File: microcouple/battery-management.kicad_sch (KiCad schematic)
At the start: 0 parts

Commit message: Finalize battery management
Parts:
- added C16, C17, C18, C19: 4.7uF, Capacitor_SMD:C_0805_2012Metric_Pad1.18x1.45mm_HandSolder, symbol Device:C
- added D66: SB5H100, Diode_SMD:D_SMB_Handsoldering, symbol Diode:SB5H100
- added D67: Charging, LED_SMD:LED_0805_2012Metric_Pad1.15x1.40mm_HandSolder, symbol Device:LED
- added D68: Done, LED_SMD:LED_0805_2012Metric_Pad1.15x1.40mm_HandSolder, symbol Device:LED
- added L1: 2.2uH, symbol Device:L
- added Q2: AO3415, Package_TO_SOT_SMD:SOT-23_Handsoldering, symbol Transistor_FET:AO3401A
- added R15: 100k, Resistor_SMD:R_0805_2012Metric_Pad1.20x1.40mm_HandSolder, symbol Device:R_US
- added R16, R17: 470R, Resistor_SMD:R_0805_2012Metric_Pad1.20x1.40mm_HandSolder, symbol Device:R_US
- added R18: 10k, Resistor_SMD:R_0805_2012Metric_Pad1.20x1.40mm_HandSolder, symbol Device:R_US
- added U5: MCP73831-2-OT, Package_TO_SOT_SMD:SOT-23-5_HandSoldering, symbol Battery_Management:MCP73831-2-OT
- added U6: LM3671MFX, Package_TO_SOT_SMD:TSOT-23-5_HandSoldering, symbol Regulator_Switching:LM3670MF
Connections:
- new net: D67.2 (A), R16.1
- new net: L1.1, U6.5 (SW)
- new net: C16.1, D66.1 (K), Q2.2 (S), U6.1 (Vin), U6.3 (EN)
- new net: D68.1 (K), R17.2
- new net: R18.1, U5.5 (PROG)
- new net +3.3V: C17.1, L1.2, U6.4 (FB)
- new net +BATT: C18.1, Q2.3 (D), U5.3 (V_{BAT})
- new net Charge Status: D67.1 (K), D68.2 (A), U5.1 (STAT)
- new net GND: C16.2, C17.2, C18.2, C19.2, R15.2, R17.1, R18.2, U5.2 (V_{SS}), U6.2 (GND)
- new net VBUS: C19.1, D66.2 (A), Q2.1 (G), R15.1, R16.2, U5.4 (V_{DD})
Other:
- note added: "https://blog.zakkemble.net/a-lithium-battery-charger-with-load-sharing/"

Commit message: Preliminary Schematic
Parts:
- C13: renamed from C18; footprint Capacitor_SMD:C_0805_2012Metric_Pad1.18x1.45mm_HandSolder -> Capacitor_SMD:C_0402_1005Metric
- C14: renamed from C19; footprint Capacitor_SMD:C_0805_2012Metric_Pad1.18x1.45mm_HandSolder -> Capacitor_SMD:C_0402_1005Metric
- C15: renamed from C16; footprint Capacitor_SMD:C_0805_2012Metric_Pad1.18x1.45mm_HandSolder -> Capacitor_SMD:C_0402_1005Metric
- C16: renamed from C17; footprint Capacitor_SMD:C_0805_2012Metric_Pad1.18x1.45mm_HandSolder -> Capacitor_SMD:C_0402_1005Metric
- D66: renamed from D67; footprint LED_SMD:LED_0805_2012Metric_Pad1.15x1.40mm_HandSolder -> LED_SMD:LED_0201_0603Metric
- D67: renamed from D68; footprint LED_SMD:LED_0805_2012Metric_Pad1.15x1.40mm_HandSolder -> LED_SMD:LED_0201_0603Metric
- L1: footprint (none) -> Inductor_SMD:L_1008_2520Metric
- R4: renamed from R16; value 470R -> 1.5k; footprint Resistor_SMD:R_0805_2012Metric_Pad1.20x1.40mm_HandSolder -> Resistor_SMD:R_0201_0603Metric
- R5: renamed from R18; footprint Resistor_SMD:R_0805_2012Metric_Pad1.20x1.40mm_HandSolder -> Resistor_SMD:R_0201_0603Metric
- R6: renamed from R17; value 470R -> 1.5k; footprint Resistor_SMD:R_0805_2012Metric_Pad1.20x1.40mm_HandSolder -> Resistor_SMD:R_0201_0603Metric
- R7: renamed from R15; footprint Resistor_SMD:R_0805_2012Metric_Pad1.20x1.40mm_HandSolder -> Resistor_SMD:R_0201_0603Metric
- renumbered D66 to D68, Q2 to Q1, U5 to U4, U6 to U5
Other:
- note removed: "https://blog.zakkemble.net/a-lithium-battery-charger-with-load-sharing/"
- company: (none) -> George Sleen
- moved on the sheet: C13, C14, C15, C16, D66, D67, D68, L1, Q1, R4, R5, R6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

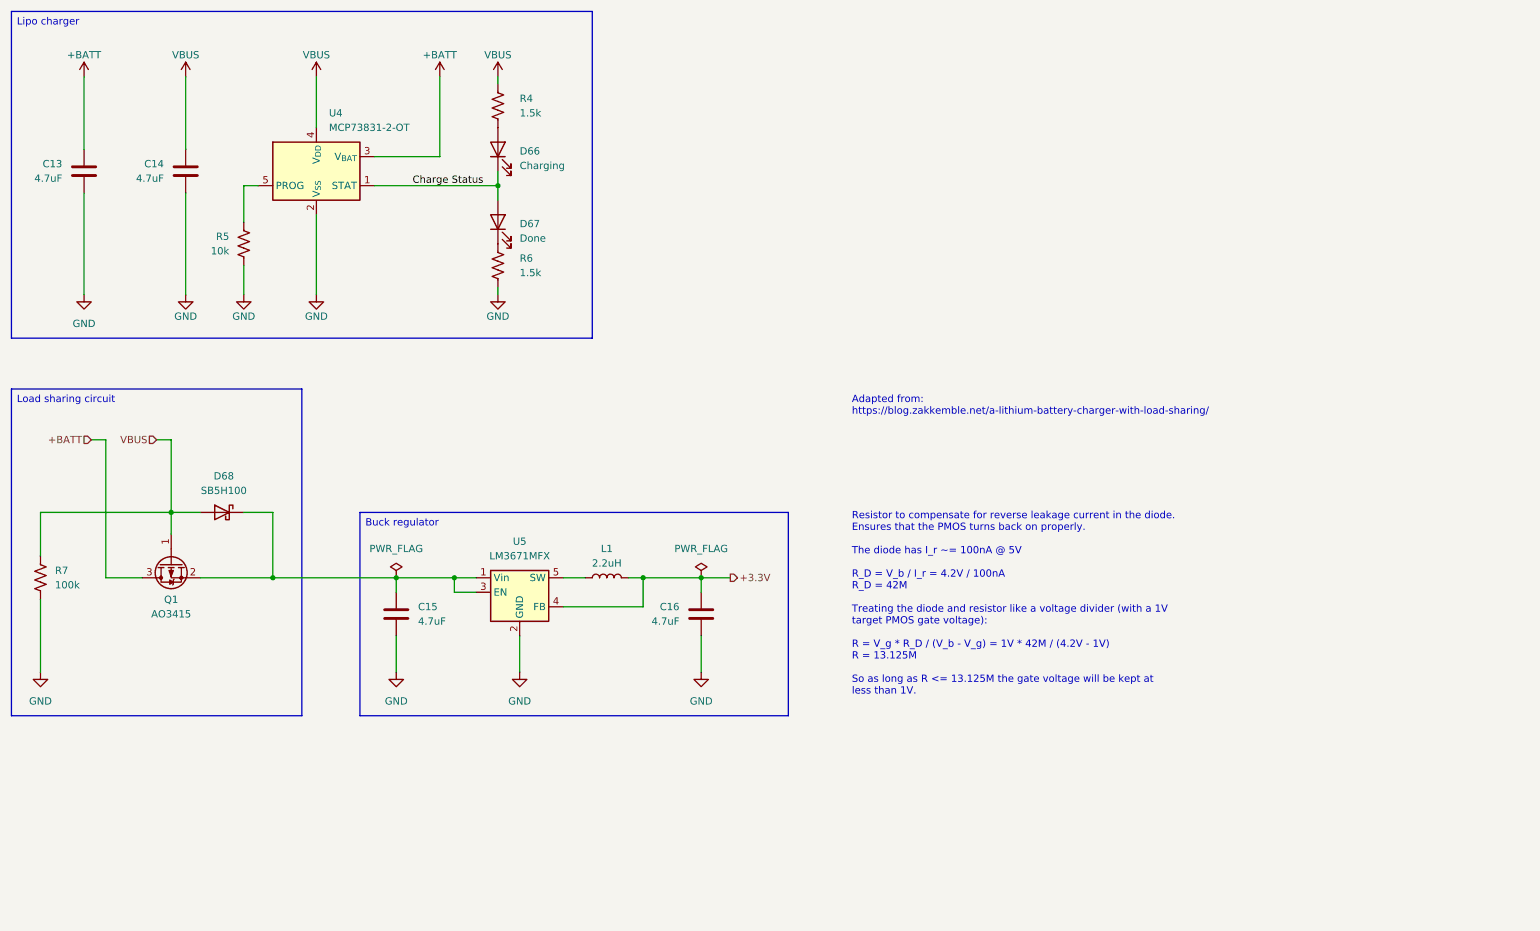
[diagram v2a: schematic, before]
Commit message: Switch THT IR components to SMD ones
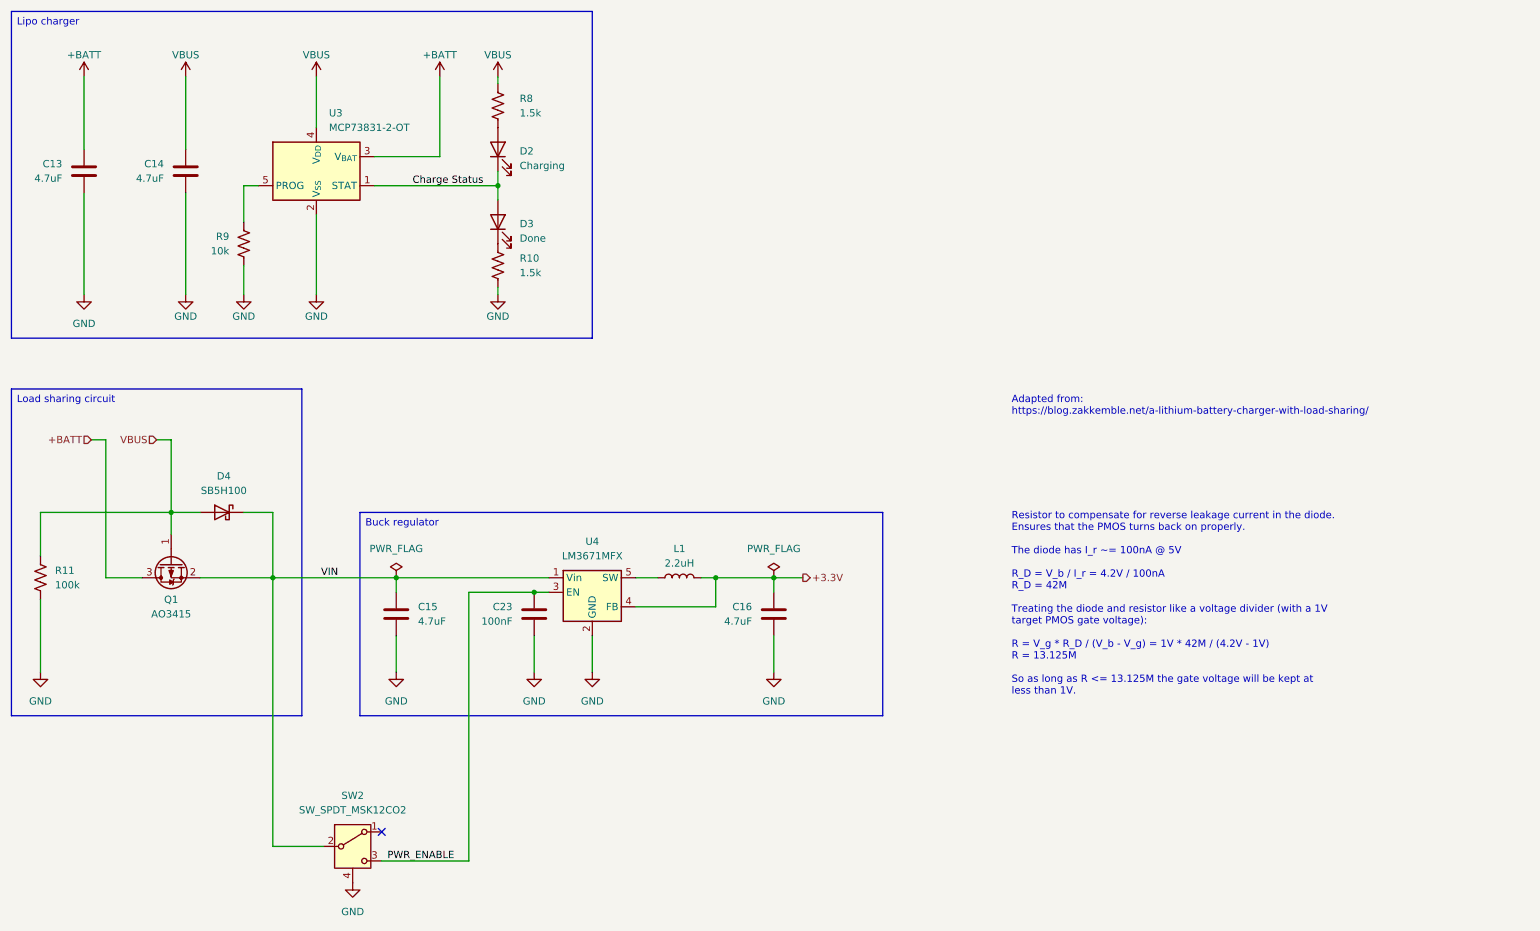
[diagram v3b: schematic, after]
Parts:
- added C23: 100nF, Capacitor_SMD:C_0201_0603Metric, symbol Device:C
- added SW2: SW_SPDT_MSK12CO2, GS_Switches:MSK12CO2, symbol GS_Switches:SW_SPDT_MSK12CO2
- D4: renamed from D68; footprint Diode_SMD:D_SMB_Handsoldering -> Diode_SMD:D_SMB
- U3: renamed from U4; footprint Package_TO_SOT_SMD:SOT-23-5_HandSoldering -> Package_TO_SOT_SMD:SOT-23-5
- U4: renamed from U5; footprint Package_TO_SOT_SMD:TSOT-23-5_HandSoldering -> Package_TO_SOT_SMD:TSOT-23-5
- renumbered D66 to D2, D67 to D3, R6 to R10, R7 to R11, R4 to R8, R5 to R9
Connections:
- net GND: now also C23.2, SW2.4 (Shield)
- net VIN: now reaches C15.1, D4.1 (K), Q1.2 (S), U4.1 (Vin)
- net VIN: now also SW2.2 (B); no longer U4.3 (EN)
- new net PWR_ENABLE: C23.1, SW2.3 (C), U4.3 (EN)
- no-connect marks 0 -> 1
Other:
- moved on the sheet: C16, L1, U4

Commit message: Preliminary layout
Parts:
- Q1: footprint Package_TO_SOT_SMD:SOT-23_Handsoldering -> Package_TO_SOT_SMD:SOT-23
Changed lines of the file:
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@@
 			)
 		)
-		(property "Footprint" "Package_TO_SOT_SMD:SOT-23_Handsoldering"
+		(property "Footprint" "Package_TO_SOT_SMD:SOT-23"
 			(at 55.245 127 0)
 			(effects

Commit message: Draft layout
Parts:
- renumbered C23 to C16, C16 to C17, D4 to D2, D2 to D3, D3 to D4, R9 to R10, R8 to R11, R10 to R12, R11 to R9
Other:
- title: (none) -> Battery Management
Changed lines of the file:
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@@
 	(paper "A4")
 	(title_block
+		(title "Battery Management")
 		(rev "A")
 		(company "George Sleen")
@@
 		(dnp no)
 		(fields_autoplaced yes)
-		(property "Reference" "D2"
+		(property "Reference" "D3"
 			(at 114.3 49.8474 90)
 			(effects
@@
 			(project ""
 				(path "/d639f16d-aedb-4af6-af94-94ea25244267/528e496b-ccc4-4c28-b7b2-36634450f252"
-					(reference "D2")
+					(reference "D3")
 					(unit 1)
 				)
@@
 		(on_board yes)
 		(dnp no)
-		(property "Reference" "#PWR049"
+		(property "Reference" "#PWR052"
 			(at 110.49 81.28 0)
 			(effects
@@
 			(project "microcouple"
 				(path "/d639f16d-aedb-4af6-af94-94ea25244267/528e496b-ccc4-4c28-b7b2-36634450f252"
-					(reference "#PWR049")
+					(reference "#PWR052")
 					(unit 1)
 				)
@@
 		(on_board yes)
 		(dnp no)
-		(property "Reference" "#PWR040"
+		(property "Reference" "#PWR041"
 			(at 38.1 40.64 0)
 			(effects
@@
 			(project "microcouple"
 				(path "/d639f16d-aedb-4af6-af94-94ea25244267/528e496b-ccc4-4c28-b7b2-36634450f252"
-					(reference "#PWR040")
+					(reference "#PWR041")
 					(unit 1)
 				)
@@
 		(on_board yes)
 		(dnp no)
-		(property "Reference" "R8"
+		(property "Reference" "R11"
 			(at 114.3 40.64 0)
 			(effects
@@
 			(project ""
 				(path "/d639f16d-aedb-4af6-af94-94ea25244267/528e496b-ccc4-4c28-b7b2-36634450f252"
-					(reference "R8")
+					(reference "R11")
 					(unit 1)
 				)
@@
 		(on_board yes)
 		(dnp no)
-		(property "Reference" "R10"
+		(property "Reference" "R12"
 			(at 114.3 68.58 0)
 			(effects
@@
 			(project "microcouple"
 				(path "/d639f16d-aedb-4af6-af94-94ea25244267/528e496b-ccc4-4c28-b7b2-36634450f252"
-					(reference "R10")
+					(reference "R12")
 					(unit 1)
 				)
@@
 		(on_board yes)
 		(dnp no)
-		(property "Reference" "D4"
+		(property "Reference" "D2"
 			(at 62.5475 106.68 0)
 			(effects
@@
 			(project ""
 				(path "/d639f16d-aedb-4af6-af94-94ea25244267/528e496b-ccc4-4c28-b7b2-36634450f252"
-					(reference "D4")
+					(reference "D2")
 					(unit 1)
 				)
@@
 		(dnp no)
 		(fields_autoplaced yes)
-		(property "Reference" "C23"
+		(property "Reference" "C16"
 			(at 113.03 129.5399 0)
 			(effects
@@
 			(project "microcouple"
 				(path "/d639f16d-aedb-4af6-af94-94ea25244267/528e496b-ccc4-4c28-b7b2-36634450f252"
-					(reference "C23")
+					(reference "C16")
 					(unit 1)
 				)
@@
 		(on_board yes)
 		(dnp no)
-		(property "Reference" "#PWR048"
+		(property "Reference" "#PWR047"
 			(at 78.74 81.28 0)
 			(effects
@@
 			(project ""
 				(path "/d639f16d-aedb-4af6-af94-94ea25244267/528e496b-ccc4-4c28-b7b2-36634450f252"
-					(reference "#PWR048")
+					(reference "#PWR047")
 					(unit 1)
 				)
@@
 		(on_board yes)
 		(dnp no)
-		(property "Reference" "#PWR042"
+		(property "Reference" "#PWR046"
 			(at 78.74 40.64 0)
 			(effects
@@
 			(project ""
 				(path "/d639f16d-aedb-4af6-af94-94ea25244267/528e496b-ccc4-4c28-b7b2-36634450f252"
-					(reference "#PWR042")
+					(reference "#PWR046")
 					(unit 1)
 				)
@@
 		(dnp no)
 		(fields_autoplaced yes)
-		(property "Reference" "#PWR050"
+		(property "Reference" "#PWR040"
 			(at 30.48 147.32 0)
 			(effects
@@
 			(project "microcouple"
 				(path "/d639f16d-aedb-4af6-af94-94ea25244267/528e496b-ccc4-4c28-b7b2-36634450f252"
-					(reference "#PWR050")
+					(reference "#PWR040")
 					(unit 1)
 				)
@@
 		(dnp no)
 		(fields_autoplaced yes)
-		(property "Reference" "#PWR053"
+		(property "Reference" "#PWR055"
 			(at 158.75 147.32 0)
 			(effects
@@
 			(project "microcouple"
 				(path "/d639f16d-aedb-4af6-af94-94ea25244267/528e496b-ccc4-4c28-b7b2-36634450f252"
-					(reference "#PWR053")
+					(reference "#PWR055")
 					(unit 1)
 				)
@@
 		(dnp no)
 		(fields_autoplaced yes)
-		(property "Reference" "#PWR051"
+		(property "Reference" "#PWR049"
 			(at 92.71 147.32 0)
 			(effects
@@
 			(project "microcouple"
 				(path "/d639f16d-aedb-4af6-af94-94ea25244267/528e496b-ccc4-4c28-b7b2-36634450f252"
-					(reference "#PWR051")
+					(reference "#PWR049")
 					(unit 1)
 				)
@@
 		(on_board yes)
 		(dnp no)
-		(property "Reference" "R11"
+		(property "Reference" "R9"
 			(at 33.02 123.1899 0)
 			(effects
@@
 			(project ""
 				(path "/d639f16d-aedb-4af6-af94-94ea25244267/528e496b-ccc4-4c28-b7b2-36634450f252"
-					(reference "R11")
+					(reference "R9")
 					(unit 1)
 				)
@@
 		(dnp no)
 		(fields_autoplaced yes)
-		(property "Reference" "#PWR074"
+		(property "Reference" "#PWR048"
 			(at 85.09 184.15 0)
 			(effects
@@
 			(project ""
 				(path "/d639f16d-aedb-4af6-af94-94ea25244267/528e496b-ccc4-4c28-b7b2-36634450f252"
-					(reference "#PWR074")
+					(reference "#PWR048")
 					(unit 1)
 				)
@@
 		(on_board yes)
 		(dnp no)
-		(property "Reference" "D3"
+		(property "Reference" "D4"
 			(at 114.3 62.5474 90)
 			(effects
@@
 			(project "microcouple"
 				(path "/d639f16d-aedb-4af6-af94-94ea25244267/528e496b-ccc4-4c28-b7b2-36634450f252"
-					(reference "D3")
+					(reference "D4")
 					(unit 1)
 				)
@@
 		(dnp no)
 		(fields_autoplaced yes)
-		(property "Reference" "#PWR052"
+		(property "Reference" "#PWR054"
 			(at 127 147.32 0)
 			(effects
@@
 			(project "microcouple"
 				(path "/d639f16d-aedb-4af6-af94-94ea25244267/528e496b-ccc4-4c28-b7b2-36634450f252"
-					(reference "#PWR052")
+					(reference "#PWR054")
 					(unit 1)
 				)
@@
 		(on_board yes)
 		(dnp no)
-		(property "Reference" "C16"
+		(property "Reference" "C17"
 			(at 154.94 129.5399 0)
 			(effects
@@
 			(project ""
 				(path "/d639f16d-aedb-4af6-af94-94ea25244267/528e496b-ccc4-4c28-b7b2-36634450f252"
-					(reference "C16")
+					(reference "C17")
 					(unit 1)
 				)
@@
 		(on_board yes)
 		(dnp no)
-		(property "Reference" "#PWR046"
+		(property "Reference" "#PWR044"
 			(at 55.88 81.28 0)
 			(effects
@@
 			(project "microcouple"
 				(path "/d639f16d-aedb-4af6-af94-94ea25244267/528e496b-ccc4-4c28-b7b2-36634450f252"
-					(reference "#PWR046")
+					(reference "#PWR044")
 					(unit 1)
 				)
@@
 		(on_board yes)
 		(dnp no)
-		(property "Reference" "#PWR047"
+		(property "Reference" "#PWR045"
 			(at 66.04 81.28 0)
 			(effects
@@
 			(project "microcouple"
 				(path "/d639f16d-aedb-4af6-af94-94ea25244267/528e496b-ccc4-4c28-b7b2-36634450f252"
-					(reference "#PWR047")
+					(reference "#PWR045")
 					(unit 1)
 				)
@@
 		(on_board yes)
 		(dnp no)
-		(property "Reference" "#PWR044"
+		(property "Reference" "#PWR051"
 			(at 110.49 40.64 0)
 			(effects
@@
 			(project "microcouple"
 				(path "/d639f16d-aedb-4af6-af94-94ea25244267/528e496b-ccc4-4c28-b7b2-36634450f252"
-					(reference "#PWR044")
+					(reference "#PWR051")
 					(unit 1)
 				)
@@
 		(on_board yes)
 		(dnp no)
-		(property "Reference" "R9"
+		(property "Reference" "R10"
 			(at 63.5 64.7699 0)
 			(effects
@@
 			(project ""
 				(path "/d639f16d-aedb-4af6-af94-94ea25244267/528e496b-ccc4-4c28-b7b2-36634450f252"
-					(reference "R9")
+					(reference "R10")
 					(unit 1)
 				)
@@
 		(dnp no)
 		(fields_autoplaced yes)
-		(property "Reference" "#PWR045"
+		(property "Reference" "#PWR042"
 			(at 38.1 81.28 0)
 			(effects
@@
 			(project "microcouple"
 				(path "/d639f16d-aedb-4af6-af94-94ea25244267/528e496b-ccc4-4c28-b7b2-36634450f252"
-					(reference "#PWR045")
+					(reference "#PWR042")
 					(unit 1)
 				)
@@
 		(on_board yes)
 		(dnp no)
-		(property "Reference" "#PWR041"
+		(property "Reference" "#PWR043"
 			(at 55.88 40.64 0)
 			(effects
@@
 			(project "microcouple"
 				(path "/d639f16d-aedb-4af6-af94-94ea25244267/528e496b-ccc4-4c28-b7b2-36634450f252"
-					(reference "#PWR041")
+					(reference "#PWR043")
 					(unit 1)
 				)
@@
 		(dnp no)
 		(fields_autoplaced yes)
-		(property "Reference" "#PWR075"
+		(property "Reference" "#PWR053"
 			(at 116.84 147.32 0)
 			(effects
@@
 			(project "microcouple"
 				(path "/d639f16d-aedb-4af6-af94-94ea25244267/528e496b-ccc4-4c28-b7b2-36634450f252"
-					(reference "#PWR075")
+					(reference "#PWR053")
 					(unit 1)
 				)
@@
 		(on_board yes)
 		(dnp no)
-		(property "Reference" "#PWR043"
+		(property "Reference" "#PWR050"
 			(at 100.33 40.64 0)
 			(effects
@@
 			(project ""
 				(path "/d639f16d-aedb-4af6-af94-94ea25244267/528e496b-ccc4-4c28-b7b2-36634450f252"
-					(reference "#PWR043")
-					(unit 1)
-				)
+					(reference "#PWR050")
+					(unit 1)
+				)

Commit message: Finish Silkscreen
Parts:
- C13, C14, C15, C17: footprint Capacitor_SMD:C_0402_1005Metric -> GS_SMD:0402_1005Metric
- C16: footprint Capacitor_SMD:C_0201_0603Metric -> GS_SMD:0201_0603Metric
- D3, D4: footprint LED_SMD:LED_0201_0603Metric -> GS_Optoelectronics:LED_0201_0603Metric
- R10, R11, R12, R9: footprint Resistor_SMD:R_0201_0603Metric -> GS_SMD:0201_0603Metric
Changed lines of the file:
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@@
 			)
 		)
-		(property "Footprint" "LED_SMD:LED_0201_0603Metric"
+		(property "Footprint" "GS_Optoelectronics:LED_0201_0603Metric"
 			(at 110.49 49.53 0)
 			(effects
@@
 			)
 		)
-		(property "Footprint" "Resistor_SMD:R_0201_0603Metric"
+		(property "Footprint" "GS_SMD:0201_0603Metric"
 			(at 109.474 41.656 90)
 			(effects
@@
 			)
 		)
-		(property "Footprint" "Resistor_SMD:R_0201_0603Metric"
+		(property "Footprint" "GS_SMD:0201_0603Metric"
 			(at 109.474 69.596 90)
 			(effects
@@
 			)
 		)
-		(property "Footprint" "Capacitor_SMD:C_0402_1005Metric"
+		(property "Footprint" "GS_SMD:0402_1005Metric"
 			(at 54.9148 57.15 0)
 			(effects
@@
 			)
 		)
-		(property "Footprint" "Capacitor_SMD:C_0201_0603Metric"
+		(property "Footprint" "GS_SMD:0201_0603Metric"
 			(at 115.8748 134.62 0)
 			(effects
@@
 			)
 		)
-		(property "Footprint" "Resistor_SMD:R_0201_0603Metric"
+		(property "Footprint" "GS_SMD:0201_0603Metric"
 			(at 31.496 124.714 90)
 			(effects
@@
 			)
 		)
-		(property "Footprint" "LED_SMD:LED_0201_0603Metric"
+		(property "Footprint" "GS_Optoelectronics:LED_0201_0603Metric"
 			(at 110.49 62.23 0)
 			(effects
@@
 			)
 		)
-		(property "Footprint" "Capacitor_SMD:C_0402_1005Metric"
+		(property "Footprint" "GS_SMD:0402_1005Metric"
 			(at 157.7848 134.62 0)
 			(effects
@@
 			)
 		)
-		(property "Footprint" "Capacitor_SMD:C_0402_1005Metric"
+		(property "Footprint" "GS_SMD:0402_1005Metric"
 			(at 93.6752 134.62 0)
 			(effects
@@
 			)
 		)
-		(property "Footprint" "Capacitor_SMD:C_0402_1005Metric"
+		(property "Footprint" "GS_SMD:0402_1005Metric"
 			(at 37.1348 57.15 0)
 			(effects
@@
 			)
 		)
-		(property "Footprint" "Resistor_SMD:R_0201_0603Metric"
+		(property "Footprint" "GS_SMD:0201_0603Metric"
 			(at 67.056 66.294 90)
 			(effects
